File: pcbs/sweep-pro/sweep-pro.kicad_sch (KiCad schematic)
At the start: 41 parts, among them SW1 SW_PUSH-kbd, SW10 SW_PUSH-kbd, SW11 SW_PUSH-kbd, SW12 SW_PUSH-kbd, SW13 SW_PUSH-kbd, SW14 SW_PUSH-kbd, SW15 SW_PUSH-kbd, SW16 SW_PUSH-kbd, SW17 SW_PUSH-kbd, SW2 SW_PUSH-kbd, SW3 SW_PUSH-kbd, SW4 SW_PUSH-kbd, SW5 SW_PUSH-kbd, SW6 SW_PUSH-kbd, SW7 SW_PUSH-kbd, SW8 SW_PUSH-kbd, SW9 SW_PUSH-kbd, U1 ProMicro-kbd

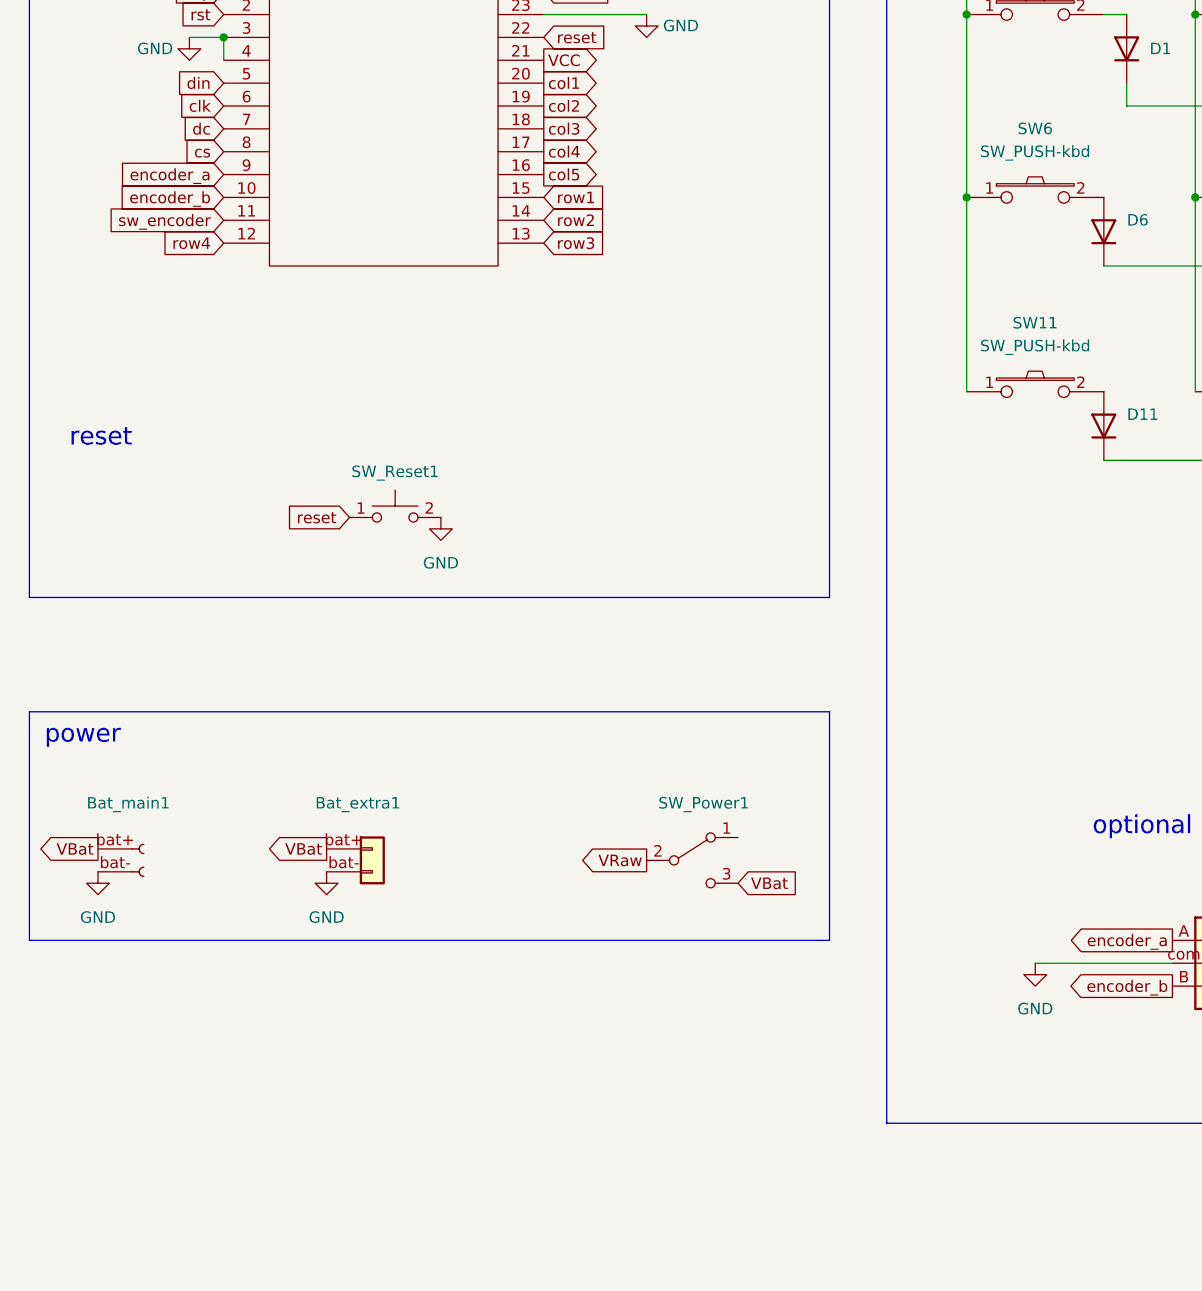
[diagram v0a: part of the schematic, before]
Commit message: first version with complete routing
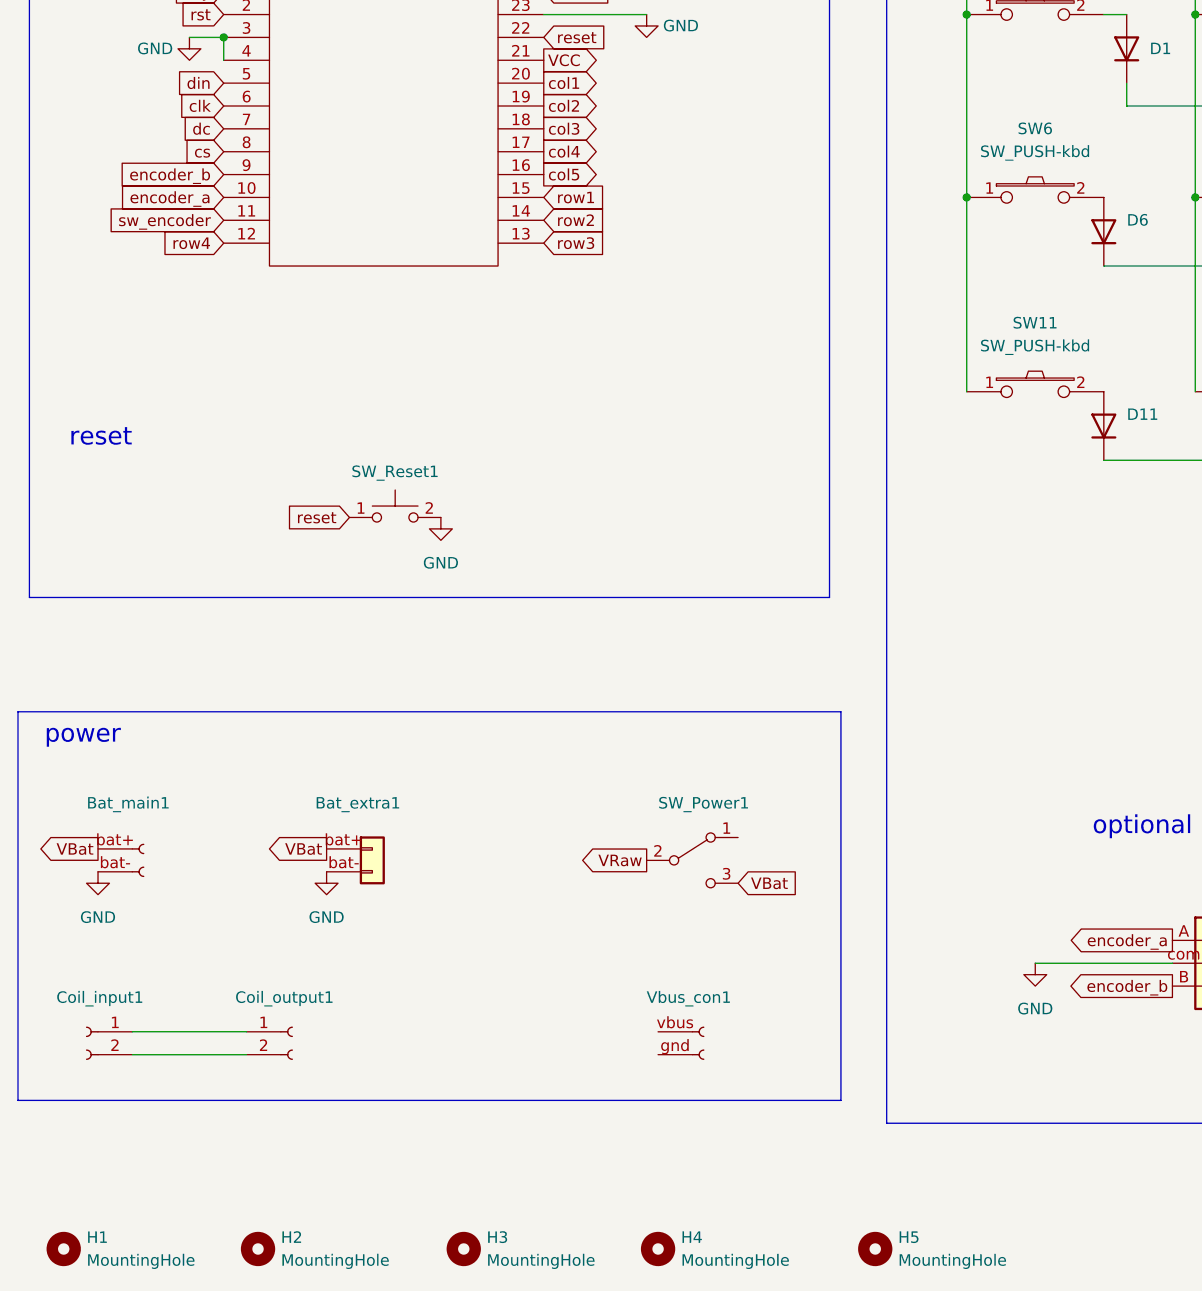
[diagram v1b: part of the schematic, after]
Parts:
- added Coil_input1, Coil_output1: Conn_01x02_Female, mylib:WirelessChager_pads_reversible, symbol Connector:Conn_01x02_Female
- added H1, H2, H3, H4, H5: MountingHole, MountingHole:MountingHole_2.2mm_M2_ISO7380_Pad_TopBottom, symbol Mechanical:MountingHole
- added Vbus_con1: Conn_01x02_Female, mylib:VBus_pad_reversible, symbol Connector:Conn_01x02_Female
- D1, D10, D11, D12, D13, D14, D15, D16, D17, D2, D3, D4, D5, D6, D7, D8, D9: footprint Diode_SMD:D_SOD-123 -> mylib:Diode_SOD-123_reversible; symbol Diode:1N4148W -> mysymbol:1N4148W
- Encoder1: footprint mylib:RollerEncoder_Panasonic_EVQWGD001 -> mylib:RollerEncoder_EVQWGD001_reversible
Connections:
- net encoder_a: now also U1.10 (E6); no longer U1.9 (D7)
- net encoder_b: now also U1.9 (D7); no longer U1.10 (E6)
- new net: Coil_input1.1 (Pin_1), Coil_output1.1 (Pin_1)
- new net: Coil_input1.2 (Pin_2), Coil_output1.2 (Pin_2)

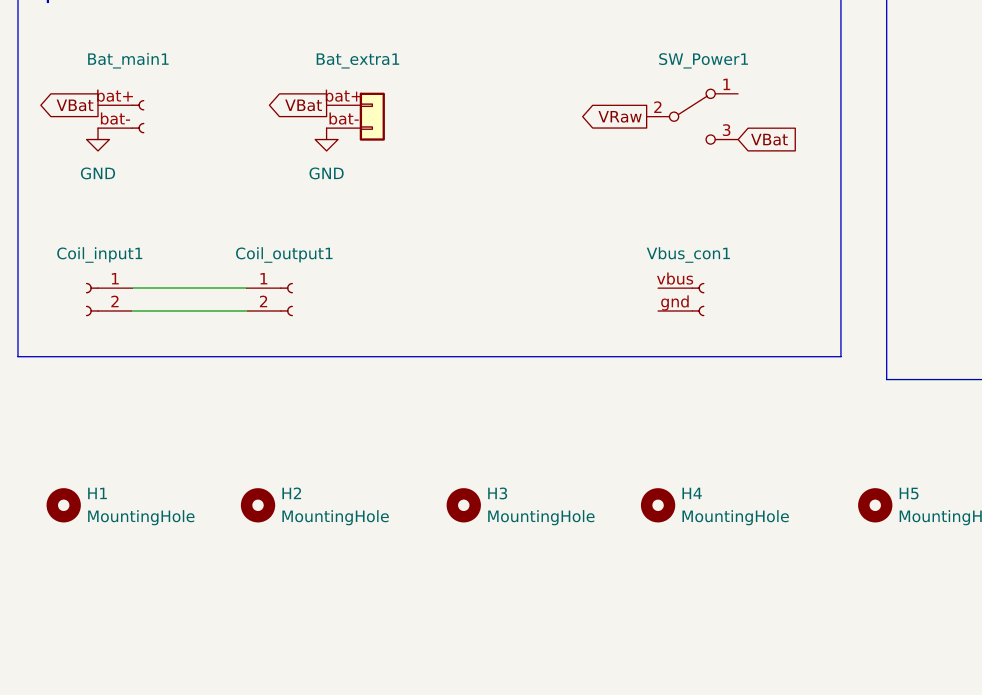
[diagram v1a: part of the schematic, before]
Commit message: outline and routing finished
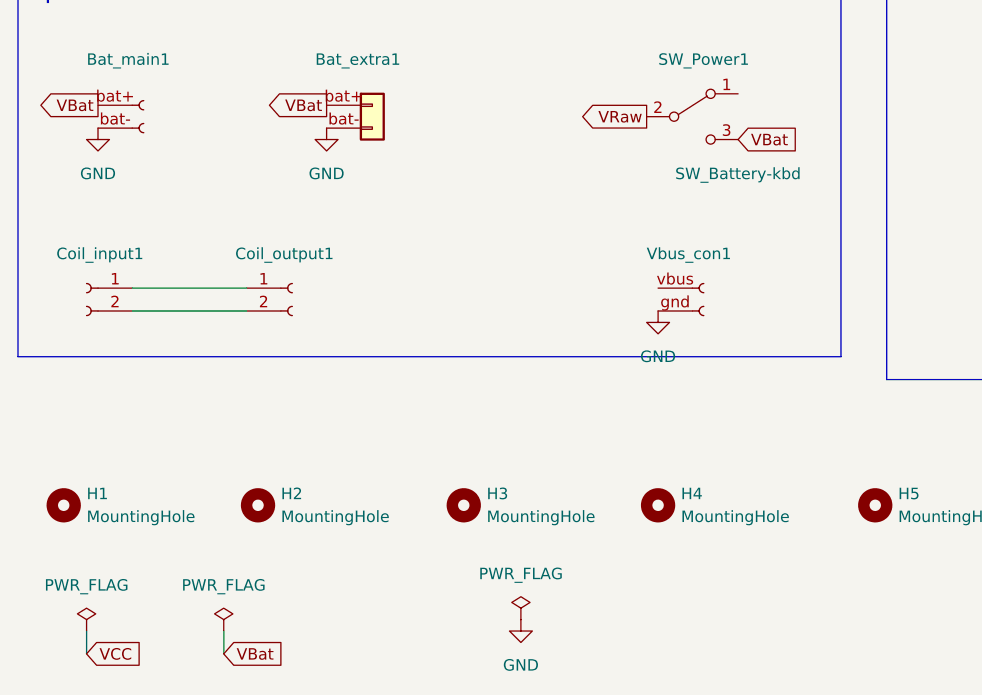
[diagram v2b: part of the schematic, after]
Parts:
- SW_Power1: value SW_Battery_kbd -> SW_Battery-kbd; symbol mysymbol:SW_Battery_kbd -> mysymbol:SW_Battery-kbd
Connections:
- net GND: now also Vbus_con1.gnd (Pin_2)
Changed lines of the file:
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@@
+    (stroke (width 0) (type default) (color 0 0 0 0))
+  )
+  (wire (pts (xy 40.64 193.04) (xy 40.64 190.5))
     (stroke (width 0) (type default) (color 0 0 0 0))
   )
@@
   )
   (polyline (pts (xy 114.3 162.56) (xy 276.86 162.56))
+    (stroke (width 0) (type default) (color 0 0 0 0))
+  )
+  (wire (pts (xy 25.4 193.04) (xy 25.4 190.5))
     (stroke (width 0) (type default) (color 0 0 0 0))
   )
@@
     )
   )
+  (global_label "VBat" (shape input) (at 40.64 193.04 0) (fields_autoplaced)
+    (effects (font (size 1.27 1.27)) (justify left))
+    (property "Intersheet References" "${INTERSHEET_REFS}" (id 0) (at 47.2864 192.9606 0)
+      (effects (font (size 1.27 1.27)) (justify left) hide)
+    )
+  )
   (global_label "cs" (shape input) (at 40.64 54.61 180) (fields_autoplaced)
     (effects (font (size 1.27 1.27)) (justify right))
@@
     )
   )
+  (global_label "VCC" (shape input) (at 25.4 193.04 0) (fields_autoplaced)
+    (effects (font (size 1.27 1.27)) (justify left))
+    (property "Intersheet References" "${INTERSHEET_REFS}" (id 0) (at 31.4417 192.9606 0)
+      (effects (font (size 1.27 1.27)) (justify left) hide)
+    )
+  )
   (global_label "sw_encoder" (shape output) (at 161.29 142.24 0) (fields_autoplaced)
     (effects (font (size 1.27 1.27)) (justify left))
@@
     (pin "1")
     (pin "2")
+  )
+  (symbol (lib_id "power:GND") (at 88.9 154.94 0) (unit 1)
+    (in_bom yes) (on_board yes) (fields_autoplaced)
+    (property "Reference" "#PWR0109" (id 0) (at 88.9 161.29 0)
+      (effects (font (size 1.27 1.27)) hide)
+    )
+    (property "Value" "GND" (id 1) (at 88.9 160.02 0))
+    (property "Footprint" "" (id 2) (at 88.9 154.94 0)
+      (effects (font (size 1.27 1.27)) hide)
+    )
+    (property "Datasheet" "" (id 3) (at 88.9 154.94 0)
+      (effects (font (size 1.27 1.27)) hide)
+    )
+    (pin "1")
   )
   (symbol (lib_id "power:GND") (at 26.67 134.62 0) (unit 1)
@@
     (pin "1")
   )
+  (symbol (lib_id "power:PWR_FLAG") (at 25.4 190.5 0) (unit 1)
+    (in_bom yes) (on_board yes) (fields_autoplaced)
+    (property "Reference" "#FLG0101" (id 0) (at 25.4 188.595 0)
+      (effects (font (size 1.27 1.27)) hide)
+    )
+    (property "Value" "PWR_FLAG" (id 1) (at 25.4 185.42 0))
+    (property "Footprint" "" (id 2) (at 25.4 190.5 0)
+      (effects (font (size 1.27 1.27)) hide)
+    )
+    (property "Datasheet" "~" (id 3) (at 25.4 190.5 0)
+      (effects (font (size 1.27 1.27)) hide)
+    )
+    (pin "1")
+  )
+  (symbol (lib_id "power:PWR_FLAG") (at 73.66 189.23 0) (unit 1)
+    (in_bom yes) (on_board yes) (fields_autoplaced)
+    (property "Reference" "#FLG0104" (id 0) (at 73.66 187.325 0)
+      (effects (font (size 1.27 1.27)) hide)
+    )
+    (property "Value" "PWR_FLAG" (id 1) (at 73.66 184.15 0))
+    (property "Footprint" "" (id 2) (at 73.66 189.23 0)
+      (effects (font (size 1.27 1.27)) hide)
+    )
+    (property "Datasheet" "~" (id 3) (at 73.66 189.23 0)
+      (effects (font (size 1.27 1.27)) hide)
+    )
+    (pin "1")
+  )
   (symbol (lib_id "power:GND") (at 36.83 41.91 0) (unit 1)
     (in_bom yes) (on_board yes)
@@
     (pin "1")
     (pin "2")
+  )
+  (symbol (lib_id "power:GND") (at 73.66 189.23 0) (unit 1)
+    (in_bom yes) (on_board yes) (fields_autoplaced)
+    (property "Reference" "#PWR0110" (id 0) (at 73.66 195.58 0)
+      (effects (font (size 1.27 1.27)) hide)
+    )
+    (property "Value" "GND" (id 1) (at 73.66 194.31 0))
+    (property "Footprint" "" (id 2) (at 73.66 189.23 0)
+      (effects (font (size 1.27 1.27)) hide)
+    )
+    (property "Datasheet" "" (id 3) (at 73.66 189.23 0)
+      (effects (font (size 1.27 1.27)) hide)
+    )
+    (pin "1")
   )
   (symbol (lib_id "mysymbol:SW_RESET-kbd") (at 59.69 95.25 0) (unit 1)
@@
     (pin "gnd")
     (pin "vbus")
+  )
+  (symbol (lib_id "power:PWR_FLAG") (at 40.64 190.5 0) (unit 1)
+    (in_bom yes) (on_board yes) (fields_autoplaced)
+    (property "Reference" "#FLG0102" (id 0) (at 40.64 188.595 0)
+      (effects (font (size 1.27 1.27)) hide)
+    )
+    (property "Value" "PWR_FLAG" (id 1) (at 40.64 185.42 0))
+    (property "Footprint" "" (id 2) (at 40.64 190.5 0)
+      (effects (font (size 1.27 1.27)) hide)
+    )
+    (property "Datasheet" "~" (id 3) (at 40.64 190.5 0)
+      (effects (font (size 1.27 1.27)) hide)
+    )
+    (pin "1")
   )
   (symbol (lib_id "mysymbol:1N4148W") (at 163.83 63.5 90) (unit 1)
@@
     (pin "2")
   )
-  (symbol (lib_id "mysymbol:SW_Battery_kbd") (at 92.71 133.35 0) (unit 1)
+  (symbol (lib_id "mysymbol:SW_Battery-kbd") (at 92.71 133.35 0) (unit 1)
     (in_bom yes) (on_board yes)
     (property "Reference" "SW_Power1" (id 0) (at 93.98 127 0))
-    (property "Value" "SW_Battery_kbd" (id 1) (at 92.71 128.27 0)
-      (effects (font (size 1.27 1.27)) hide)
-    )
+    (property "Value" "SW_Battery-kbd" (id 1) (at 97.79 139.7 0))
     (property "Footprint" "mylib:Power_reversible" (id 2) (at 92.71 133.35 0)
       (effects (font (size 1.27 1.27)) hide)
@@
     (pin "2")
   )
-  (symbol (lib_name "MountingHole_3") (lib_id "Mechanical:MountingHole") (at 22.86 176.53 0) (unit 1)
+  (symbol (lib_id "Mechanical:MountingHole") (at 22.86 176.53 0) (unit 1)
     (in_bom no) (on_board yes) (fields_autoplaced)
     (property "Reference" "H1" (id 0) (at 25.4 175.2599 0)
@@
   )
   (symbol_instances
+    (path "/68d67422-3508-4c5d-b374-de95b28473c0"
+      (reference "#FLG0101") (unit 1) (value "PWR_FLAG") (footprint "")
+    )
+    (path "/7ec3bc2d-f701-4008-a0ce-ebee0f1fe794"
+      (reference "#FLG0102") (unit 1) (value "PWR_FLAG") (footprint "")
+    )
+    (path "/69092605-a59d-481b-b814-56b2eadaeaff"
+      (reference "#FLG0104") (unit 1) (value "PWR_FLAG") (footprint "")
+    )
     (path "/855c99ea-116b-461a-b2c3-0fdecc143018"
       (reference "#PWR0101") (unit 1) (value "GND") (footprint "")
@@
       (reference "#PWR0108") (unit 1) (value "GND") (footprint "")
     )
+    (path "/1ccaf9c1-07e5-4528-834a-88b5e92cc69d"
+      (reference "#PWR0109") (unit 1) (value "GND") (footprint "")
+    )
+    (path "/6dfb8131-ca0e-42be-a304-9ed244979805"
+      (reference "#PWR0110") (unit 1) (value "GND") (footprint "")
+    )
     (path "/5a75c756-d045-47cd-91a8-22173b1f50b9"
       (reference "Bat_extra1") (unit 1) (value "Conn_Battery_pluggable") (footprint "mylib:Battery_connector_lim_reversible")
@@
     )
     (path "/e6eab363-1559-4ffc-8b52-40128dbb1fb9"
-      (reference "SW_Power1") (unit 1) (value "SW_Battery_kbd") (footprint "mylib:Power_reversible")
+      (reference "SW_Power1") (unit 1) (value "SW_Battery-kbd") (footprint "mylib:Power_reversible")
     )
     (path "/701bde1d-fc7b-4f57-824d-75982cb3ba5e"
